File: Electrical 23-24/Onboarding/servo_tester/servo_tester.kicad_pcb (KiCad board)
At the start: 2 copper layers, 28.4 x 79.2 mm, 18 parts, among them J1 Servo 1, J2 Servo 2, J3 Power In, J4 Prog, J5 Servo 3, SW1 RotaryEncoder_Switch, U1 ATtiny404-SS, U2 AP2205-33Y-13, U3 PCF8551ATT_AJ, U4 VIM-878-DP-FC-S-LV

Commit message: Finish servo tester silk
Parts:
- added G***: LOGO, LOGO, B.Cu at (114.6, 100.1)
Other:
- board text added: "+"
- board text added: "-"
- board text added: "1"
- board text added: "2"
- board text added: "3"
- board text added: "3V3"
- board text added: "CCW"
- board text added: "CW"
- board text added: "GND"
- board text added: "RX"
- board text added: "SERVO TESTER v1.0"
- board text added: "TX"
- board text added: "UPDI"
- board text added: "VIN 0-3S"
- board text added: "~"

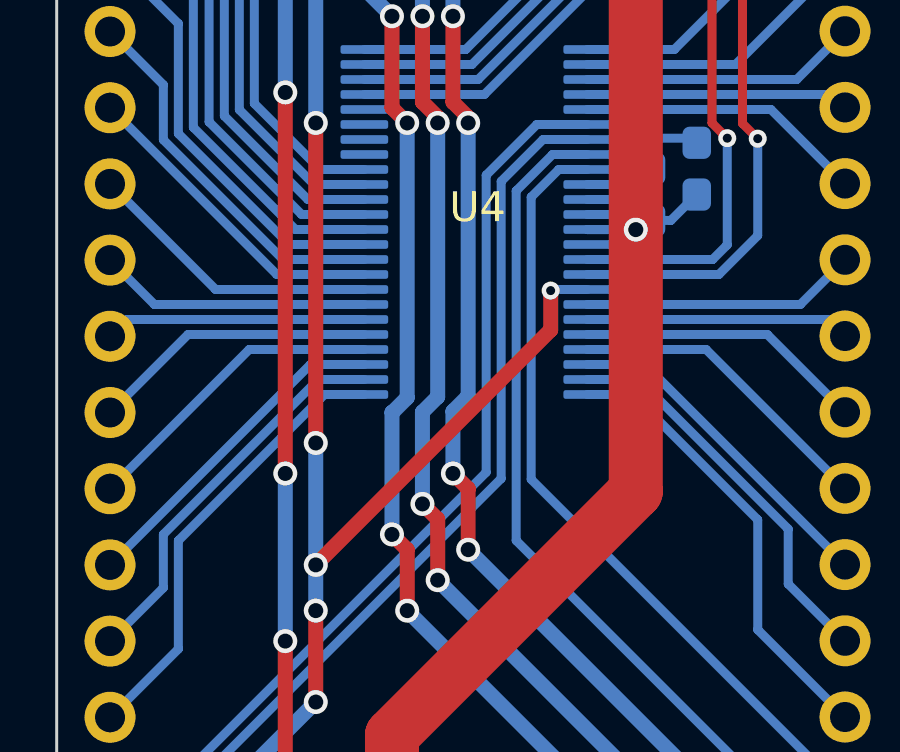
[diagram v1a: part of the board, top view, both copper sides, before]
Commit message: Updated folders and schematic for onboarding
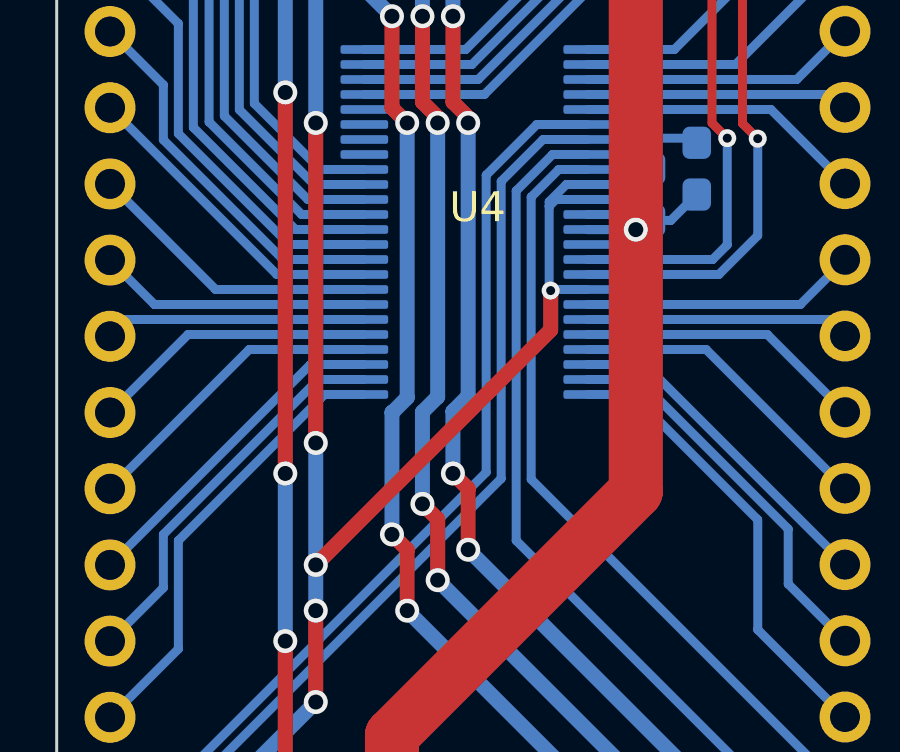
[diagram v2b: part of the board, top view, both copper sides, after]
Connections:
- C3 pad 1: Net-(U3-VDD) -> 3V3
- C4 pad 1: Net-(U3-VLCD) -> 3V3
- U3 pad 10: Net-(U3-VLCD) -> 3V3
- U3 pad 11: Net-(U3-VDD) -> 3V3
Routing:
- net 3V3: track 111.6 -> 124.9 mm
- net Net-(U3-VLCD): track 4.83 -> 0.00 mm
- net Net-(U3-VDD): track 2.55 -> 0.00 mm
